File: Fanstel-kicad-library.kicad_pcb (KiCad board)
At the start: 2 copper layers, 7 parts, among them U1 BC832-V0, U2 BT832L, U3 BC832-V1, U4 BM832, U5 BT832X, U6 BM840, U7 BT840

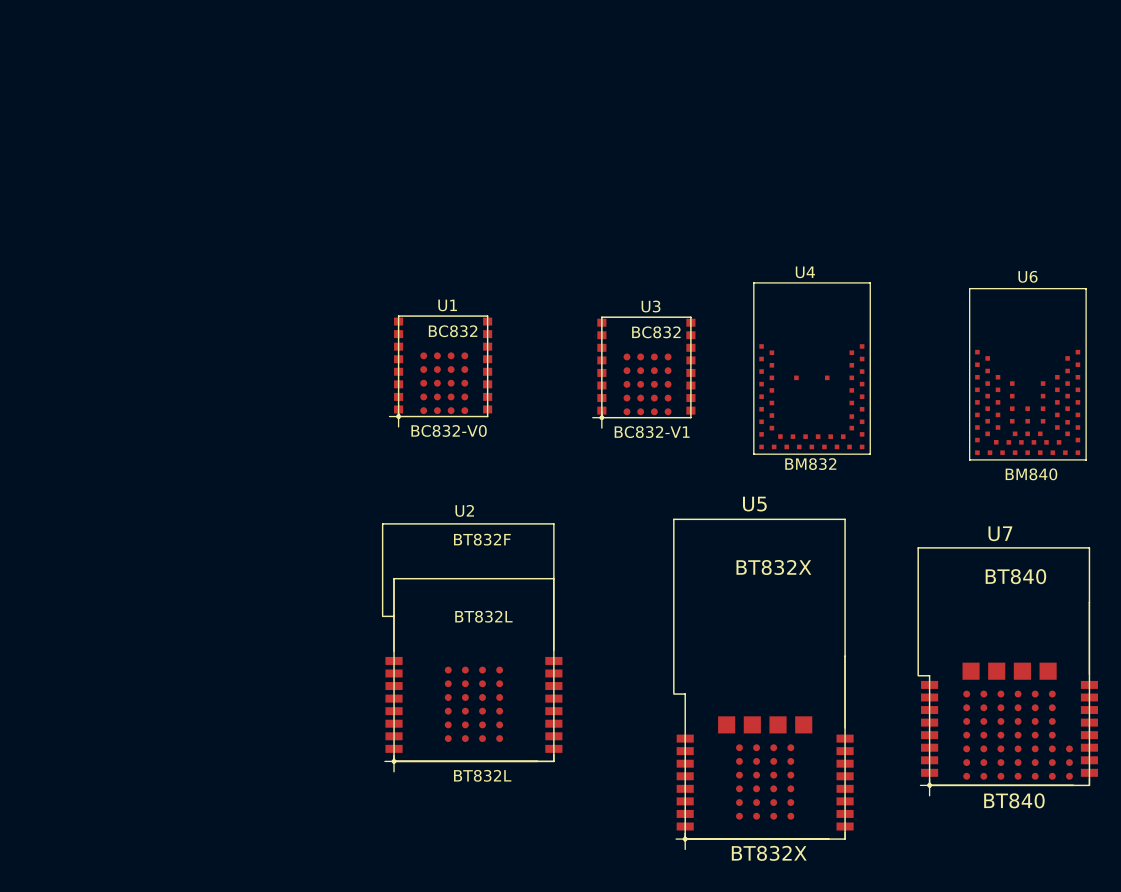
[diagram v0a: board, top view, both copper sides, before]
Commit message: Adds BC805 ( #3 ) and BT40F ( #4 )
Added two new modules and updated the preview image for readme
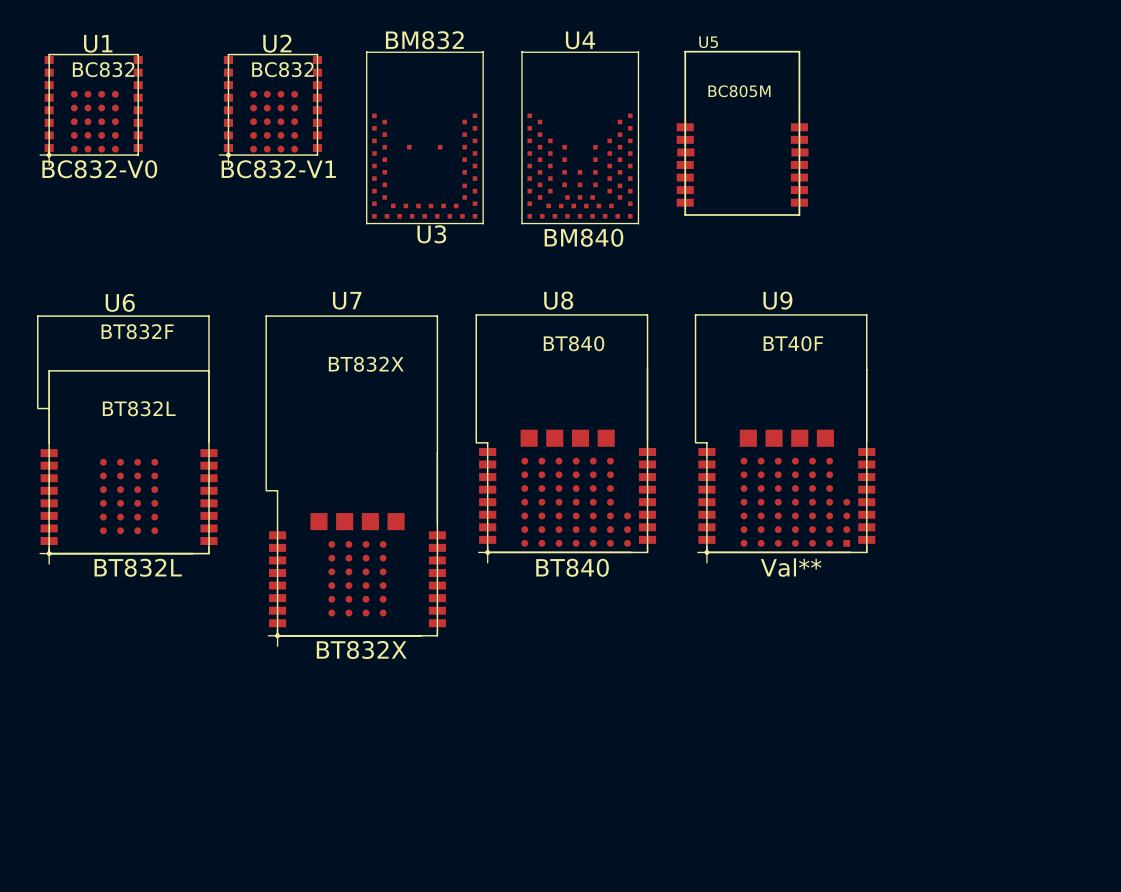
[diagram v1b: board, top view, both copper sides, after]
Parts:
- added U8: BT840, Fanstel_modules:BT840-BT840, F.Cu at (130.2, 94.8)
- added U9: Val**, Fanstel_modules:BT40F, F.Cu at (149.4, 94.8)
- U2: value BT832L -> BC832-V1; footprint Fanstel_modules:BT832-BT832L -> Fanstel_modules:BC832-BC832
- U3: value BC832-V1 -> BM832; footprint Fanstel_modules:BC832-BC832 -> Fanstel_modules:BM832-1-BM832
- U4: value BM832 -> BM840; footprint Fanstel_modules:BM832-1-BM832 -> Fanstel_modules:BM840-1-BM840
- U5: value BT832X -> BC805M; footprint Fanstel_modules:BT832X-BT832X -> Fanstel_modules:BC805M
- U6: value BM840 -> BT832L; footprint Fanstel_modules:BM840-1-BM840 -> Fanstel_modules:BT832-BT832L
- U7: value BT840 -> BT832X; footprint Fanstel_modules:BT840-BT840 -> Fanstel_modules:BT832X-BT832X
- moved U6 81.0 mm to (91.8, 94.9)
- moved U7 58.6 mm to (111.8, 102.1)
- moved U2 55.0 mm to (107.5, 60.0)
- moved U5 54.7 mm to (147.5, 65.2)
- moved U1 38.2 mm to (91.8, 60.0)
- moved U4 28.6 mm to (133.2, 66.0)
- moved U3 26.7 mm to (119.6, 66.0)
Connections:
- U1 pad P$1: (no net) -> Net-(U1-PadP$1)
- U1 pad P$10: (no net) -> Net-(U1-PadP$10)
- U1 pad P$11: (no net) -> Net-(U1-PadP$11)
- U1 pad P$12: (no net) -> Net-(U1-PadP$12)
- U1 pad P$13: (no net) -> Net-(U1-PadP$13)
- U1 pad P$14: (no net) -> Net-(U1-PadP$14)
- U1 pad P$15: (no net) -> Net-(U1-PadP$15)
- U1 pad P$16: (no net) -> Net-(U1-PadP$16)
- U1 pad P$2: (no net) -> Net-(U1-PadP$2)
- U1 pad P$3: (no net) -> Net-(U1-PadP$3)
- U1 pad P$4: (no net) -> Net-(U1-PadP$4)
- U1 pad P$5: (no net) -> Net-(U1-PadP$5)
- U1 pad P$6: (no net) -> Net-(U1-PadP$6)
- U1 pad P$7: (no net) -> Net-(U1-PadP$7)
- U1 pad P$8: (no net) -> Net-(U1-PadP$8)
- U1 pad P$9: (no net) -> Net-(U1-PadP$9)
- U1 pad P$A1: (no net) -> Net-(U1-PadP$A1)
- U1 pad P$A2: (no net) -> Net-(U1-PadP$A2)
- U1 pad P$A3: (no net) -> Net-(U1-PadP$A3)
- U1 pad P$A4: (no net) -> Net-(U1-PadP$A4)
- U1 pad P$A5: (no net) -> Net-(U1-PadP$A5)
- U1 pad P$B1: (no net) -> Net-(U1-PadP$B1)
- U1 pad P$B2: (no net) -> Net-(U1-PadP$B2)
- U1 pad P$B3: (no net) -> Net-(U1-PadP$B3)
- U1 pad P$B4: (no net) -> Net-(U1-PadP$B4)
- U1 pad P$B5: (no net) -> Net-(U1-PadP$B5)
- U1 pad P$C1: (no net) -> Net-(U1-PadP$C1)
- U1 pad P$C2: (no net) -> Net-(U1-PadP$C2)
- U1 pad P$C3: (no net) -> Net-(U1-PadP$C3)
- U1 pad P$C4: (no net) -> Net-(U1-PadP$C4)
- U1 pad P$C5: (no net) -> Net-(U1-PadP$C5)
- U1 pad P$D1: (no net) -> Net-(U1-PadP$D1)
- U1 pad P$D2: (no net) -> Net-(U1-PadP$D2)
- U1 pad P$D3: (no net) -> Net-(U1-PadP$D3)
- U1 pad P$D4: (no net) -> Net-(U1-PadP$D4)
- U1 pad P$D5: (no net) -> Net-(U1-PadP$D5)
- U2 pad P$1: (no net) -> Net-(U2-PadP$1)
- U2 pad P$10: (no net) -> Net-(U2-PadP$10)
- U2 pad P$11: (no net) -> Net-(U2-PadP$11)
- U2 pad P$12: (no net) -> Net-(U2-PadP$12)
- U2 pad P$13: (no net) -> Net-(U2-PadP$13)
- U2 pad P$14: (no net) -> Net-(U2-PadP$14)
- U2 pad P$15: (no net) -> Net-(U2-PadP$15)
- U2 pad P$16: (no net) -> Net-(U2-PadP$16)
- U2 pad P$2: (no net) -> Net-(U2-PadP$2)
- U2 pad P$3: (no net) -> Net-(U2-PadP$3)
- U2 pad P$4: (no net) -> Net-(U2-PadP$4)
- U2 pad P$5: (no net) -> Net-(U2-PadP$5)
- U2 pad P$6: (no net) -> Net-(U2-PadP$6)
- U2 pad P$7: (no net) -> Net-(U2-PadP$7)
- U2 pad P$8: (no net) -> Net-(U2-PadP$8)
- U2 pad P$9: (no net) -> Net-(U2-PadP$9)
- U2 pad P$A1: (no net) -> Net-(U2-PadP$A1)
- U2 pad P$A2: (no net) -> Net-(U2-PadP$A2)
- U2 pad P$A3: (no net) -> Net-(U2-PadP$A3)
- U2 pad P$A4: (no net) -> Net-(U2-PadP$A4)
- U2 pad P$A5: (no net) -> Net-(U2-PadP$A5)
- U2 pad P$B1: (no net) -> Net-(U2-PadP$B1)
- U2 pad P$B2: (no net) -> Net-(U2-PadP$B2)
- U2 pad P$B3: (no net) -> Net-(U2-PadP$B3)
- U2 pad P$B4: (no net) -> Net-(U2-PadP$B4)
- U2 pad P$B5: (no net) -> Net-(U2-PadP$B5)
- U2 pad P$C1: (no net) -> Net-(U2-PadP$C1)
- U2 pad P$C2: (no net) -> Net-(U2-PadP$C2)
- U2 pad P$C3: (no net) -> Net-(U2-PadP$C3)
- U2 pad P$C4: (no net) -> Net-(U2-PadP$C4)
- U2 pad P$C5: (no net) -> Net-(U2-PadP$C5)
- U2 pad P$D1: (no net) -> Net-(U2-PadP$D1)
- U2 pad P$D2: (no net) -> Net-(U2-PadP$D2)
- U2 pad P$D3: (no net) -> Net-(U2-PadP$D3)
- U2 pad P$D4: (no net) -> Net-(U2-PadP$D4)
- U2 pad P$D5: (no net) -> Net-(U2-PadP$D5)
- U3 pad P$1: (no net) -> Net-(U3-PadP$1)
- U3 pad P$10: (no net) -> Net-(U3-PadP$10)
- U3 pad P$11: (no net) -> Net-(U3-PadP$11)
- U3 pad P$12: (no net) -> Net-(U3-PadP$12)
- U3 pad P$13: (no net) -> Net-(U3-PadP$13)
- U3 pad P$14: (no net) -> Net-(U3-PadP$14)
- U3 pad P$15: (no net) -> Net-(U3-PadP$15)
- U3 pad P$16: (no net) -> Net-(U3-PadP$16)
- U3 pad P$2: (no net) -> Net-(U3-PadP$2)
- U3 pad P$3: (no net) -> Net-(U3-PadP$3)
- U3 pad P$4: (no net) -> Net-(U3-PadP$4)
- U3 pad P$5: (no net) -> Net-(U3-PadP$5)
- U3 pad P$6: (no net) -> Net-(U3-PadP$6)
- U3 pad P$7: (no net) -> Net-(U3-PadP$7)
- U3 pad P$8: (no net) -> Net-(U3-PadP$8)
- U3 pad P$9: (no net) -> Net-(U3-PadP$9)
- U4 pad P$1: (no net) -> Net-(U4-PadP$1)
- U4 pad P$10: (no net) -> Net-(U4-PadP$10)
- U4 pad P$11: (no net) -> Net-(U4-PadP$11)
- U4 pad P$12: (no net) -> Net-(U4-PadP$12)
- U4 pad P$13: (no net) -> Net-(U4-PadP$13)
- U4 pad P$14: (no net) -> Net-(U4-PadP$14)
- U4 pad P$15: (no net) -> Net-(U4-PadP$15)
- U4 pad P$16: (no net) -> Net-(U4-PadP$16)
- U4 pad P$17: (no net) -> Net-(U4-PadP$17)
- U4 pad P$18: (no net) -> Net-(U4-PadP$18)
- U4 pad P$19: (no net) -> Net-(U4-PadP$19)
- U4 pad P$2: (no net) -> Net-(U4-PadP$2)
- U4 pad P$20: (no net) -> Net-(U4-PadP$20)
- U4 pad P$21: (no net) -> Net-(U4-PadP$21)
- U4 pad P$22: (no net) -> Net-(U4-PadP$22)
- U4 pad P$23: (no net) -> Net-(U4-PadP$23)
- U4 pad P$24: (no net) -> Net-(U4-PadP$24)
- U4 pad P$25: (no net) -> Net-(U4-PadP$25)
- U4 pad P$26: (no net) -> Net-(U4-PadP$26)
- U4 pad P$27: (no net) -> Net-(U4-PadP$27)
- U4 pad P$28: (no net) -> Net-(U4-PadP$28)
- U4 pad P$29: (no net) -> Net-(U4-PadP$29)
- U4 pad P$3: (no net) -> Net-(U4-PadP$3)
- U4 pad P$30: (no net) -> Net-(U4-PadP$30)
- U4 pad P$31: (no net) -> Net-(U4-PadP$31)
- U4 pad P$32: (no net) -> Net-(U4-PadP$32)
- U4 pad P$33: (no net) -> Net-(U4-PadP$33)
- U4 pad P$34: (no net) -> Net-(U4-PadP$34)
- U4 pad P$35: (no net) -> Net-(U4-PadP$35)
- U4 pad P$36: (no net) -> Net-(U4-PadP$36)
- U4 pad P$37: (no net) -> Net-(U4-PadP$37)
- U4 pad P$38: (no net) -> Net-(U4-PadP$38)
- U4 pad P$39: (no net) -> Net-(U4-PadP$39)
- U4 pad P$4: (no net) -> Net-(U4-PadP$4)
- U4 pad P$40: (no net) -> Net-(U4-PadP$40)
- U4 pad P$41: (no net) -> Net-(U4-PadP$41)
- U4 pad P$42: (no net) -> Net-(U4-PadP$42)
- U4 pad P$43: (no net) -> Net-(U4-PadP$43)
- U4 pad P$44: (no net) -> Net-(U4-PadP$44)
- U4 pad P$45: (no net) -> Net-(U4-PadP$45)
- U4 pad P$46: (no net) -> Net-(U4-PadP$46)
- U4 pad P$47: (no net) -> Net-(U4-PadP$47)
- U4 pad P$5: (no net) -> Net-(U4-PadP$5)
- U4 pad P$6: (no net) -> Net-(U4-PadP$6)
- U4 pad P$7: (no net) -> Net-(U4-PadP$7)
- U4 pad P$8: (no net) -> Net-(U4-PadP$8)
- U4 pad P$9: (no net) -> Net-(U4-PadP$9)
- U6 pad P$1: (no net) -> Net-(U6-PadP$1)
- U6 pad P$10: (no net) -> Net-(U6-PadP$10)
- U6 pad P$11: (no net) -> Net-(U6-PadP$11)
- U6 pad P$12: (no net) -> Net-(U6-PadP$12)
- U6 pad P$13: (no net) -> Net-(U6-PadP$13)
- U6 pad P$14: (no net) -> Net-(U6-PadP$14)
- U6 pad P$15: (no net) -> Net-(U6-PadP$15)
- U6 pad P$16: (no net) -> Net-(U6-PadP$16)
- U6 pad P$2: (no net) -> Net-(U6-PadP$2)
- U6 pad P$3: (no net) -> Net-(U6-PadP$3)
- U6 pad P$4: (no net) -> Net-(U6-PadP$4)
- U6 pad P$5: (no net) -> Net-(U6-PadP$5)
- U6 pad P$6: (no net) -> Net-(U6-PadP$6)
- U6 pad P$7: (no net) -> Net-(U6-PadP$7)
- U6 pad P$8: (no net) -> Net-(U6-PadP$8)
- U6 pad P$9: (no net) -> Net-(U6-PadP$9)
- U7 pad P$1: (no net) -> Net-(U7-PadP$1)
- U7 pad P$10: (no net) -> Net-(U7-PadP$10)
- U7 pad P$11: (no net) -> Net-(U7-PadP$11)
- U7 pad P$12: (no net) -> Net-(U7-PadP$12)
- U7 pad P$13: (no net) -> Net-(U7-PadP$13)
- U7 pad P$14: (no net) -> Net-(U7-PadP$14)
- U7 pad P$15: (no net) -> Net-(U7-PadP$15)
- U7 pad P$16: (no net) -> Net-(U7-PadP$16)
- U7 pad P$2: (no net) -> Net-(U7-PadP$2)
- U7 pad P$3: (no net) -> Net-(U7-PadP$3)
- U7 pad P$4: (no net) -> Net-(U7-PadP$4)
- U7 pad P$5: (no net) -> Net-(U7-PadP$5)
- U7 pad P$6: (no net) -> Net-(U7-PadP$6)
- U7 pad P$7: (no net) -> Net-(U7-PadP$7)
- U7 pad P$8: (no net) -> Net-(U7-PadP$8)
- U7 pad P$9: (no net) -> Net-(U7-PadP$9)
- U7 pad P$A0: (no net) -> Net-(U7-PadP$A0)
- U7 pad P$A1: (no net) -> Net-(U7-PadP$A1)
- U7 pad P$A2: (no net) -> Net-(U7-PadP$A2)
- U7 pad P$A3: (no net) -> Net-(U7-PadP$A3)
- U7 pad P$A4: (no net) -> Net-(U7-PadP$A4)
- U7 pad P$A5: (no net) -> Net-(U7-PadP$A5)
- U7 pad P$B0: (no net) -> Net-(U7-PadP$B0)
- U7 pad P$B1: (no net) -> Net-(U7-PadP$B1)
- U7 pad P$B2: (no net) -> Net-(U7-PadP$B2)
- U7 pad P$B3: (no net) -> Net-(U7-PadP$B3)
- U7 pad P$B4: (no net) -> Net-(U7-PadP$B4)
- U7 pad P$B5: (no net) -> Net-(U7-PadP$B5)
- U7 pad P$C0: (no net) -> Net-(U7-PadP$C0)
- U7 pad P$C1: (no net) -> Net-(U7-PadP$C1)
- U7 pad P$C2: (no net) -> Net-(U7-PadP$C2)
- U7 pad P$C3: (no net) -> Net-(U7-PadP$C3)
- U7 pad P$C4: (no net) -> Net-(U7-PadP$C4)
- U7 pad P$C5: (no net) -> Net-(U7-PadP$C5)
- U7 pad P$D0: (no net) -> Net-(U7-PadP$D0)
- U7 pad P$D1: (no net) -> Net-(U7-PadP$D1)
- U7 pad P$D2: (no net) -> Net-(U7-PadP$D2)
- U7 pad P$D3: (no net) -> Net-(U7-PadP$D3)
- U7 pad P$D4: (no net) -> Net-(U7-PadP$D4)
- U7 pad P$D5: (no net) -> Net-(U7-PadP$D5)
- U7 pad P$F0: (no net) -> Net-(U7-PadP$F0)
- U7 pad P$F1: (no net) -> Net-(U7-PadP$F1)
- U7 pad P$F2: (no net) -> Net-(U7-PadP$F2)
- U7 pad P$F3: (no net) -> Net-(U7-PadP$F3)

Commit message: Fix Val** issue in preview
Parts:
- U9: value Val** -> BT40F
